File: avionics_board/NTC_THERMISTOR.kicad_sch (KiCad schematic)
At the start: 2 parts

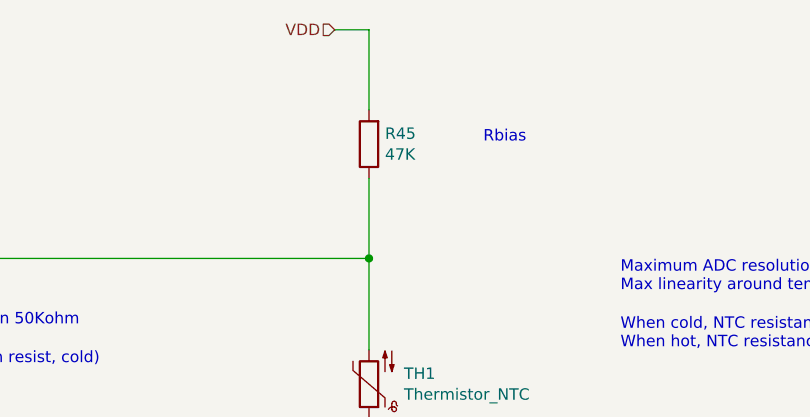
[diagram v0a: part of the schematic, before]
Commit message: change form factor to 80x80 and cleanup pcb
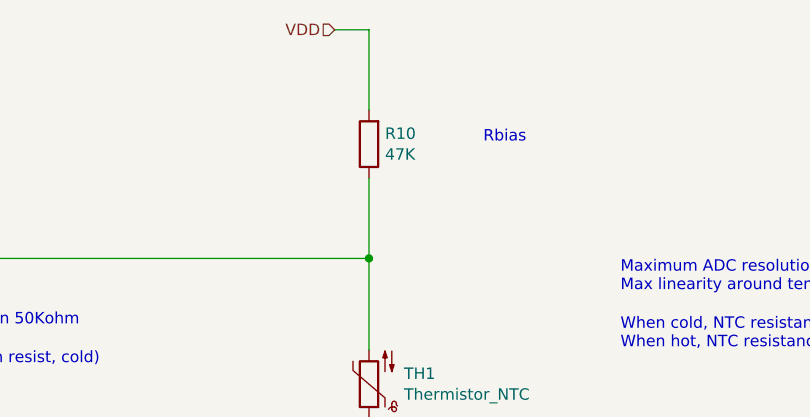
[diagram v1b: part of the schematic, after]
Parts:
- renumbered R45 to R10
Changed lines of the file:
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@@
 		(on_board yes)
 		(dnp no)
-		(property "Reference" "R45"
+		(property "Reference" "R10"
 			(at 122.428 47.0916 0)
 			(effects
@@
 			(project ""
 				(path "/f6cc00ab-17f1-4973-862f-7ac95fe70668/00000000-0000-0000-0000-00005ea31c93/00000000-0000-0000-0000-00005eab0b79/00000000-0000-0000-0000-00005eb419ee"
-					(reference "R45")
+					(reference "R10")
 					(unit 1)
 				)
 				(path "/f6cc00ab-17f1-4973-862f-7ac95fe70668/00000000-0000-0000-0000-00005ea31c93/00000000-0000-0000-0000-00005eab0b79/00000000-0000-0000-0000-00005ec0237f"
-					(reference "R46")
+					(reference "R11")
 					(unit 1)
 				)
 				(path "/f6cc00ab-17f1-4973-862f-7ac95fe70668/00000000-0000-0000-0000-00005ea31c93/00000000-0000-0000-0000-00005eab0b79/00000000-0000-0000-0000-00005ec02646"
-					(reference "R47")
+					(reference "R12")
 					(unit 1)
 				)
 				(path "/f6cc00ab-17f1-4973-862f-7ac95fe70668/00000000-0000-0000-0000-00005ea31c93/00000000-0000-0000-0000-00005eab0b79/00000000-0000-0000-0000-00005ec0264b"
-					(reference "R48")
+					(reference "R13")
 					(unit 1)
 				)
 				(path "/f6cc00ab-17f1-4973-862f-7ac95fe70668/00000000-0000-0000-0000-00005ea31c93/00000000-0000-0000-0000-00005eab0b79/00000000-0000-0000-0000-00005ec02e34"
-					(reference "R49")
+					(reference "R14")
 					(unit 1)
 				)
 				(path "/f6cc00ab-17f1-4973-862f-7ac95fe70668/00000000-0000-0000-0000-00005ea31c93/00000000-0000-0000-0000-00005eab0b79/00000000-0000-0000-0000-00005ec02e39"
-					(reference "R50")
+					(reference "R15")
 					(unit 1)
 				)
 				(path "/f6cc00ab-17f1-4973-862f-7ac95fe70668/00000000-0000-0000-0000-00005ea31c93/00000000-0000-0000-0000-00005eab0b79/00000000-0000-0000-0000-00005ec02e3e"
-					(reference "R51")
+					(reference "R16")
 					(unit 1)
 				)
 				(path "/f6cc00ab-17f1-4973-862f-7ac95fe70668/00000000-0000-0000-0000-00005ea31c93/00000000-0000-0000-0000-00005eab0b79/00000000-0000-0000-0000-00005ec02e43"
-					(reference "R52")
+					(reference "R17")
 					(unit 1)
 				)

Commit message: AV: small cleanup, USB, and CAN power
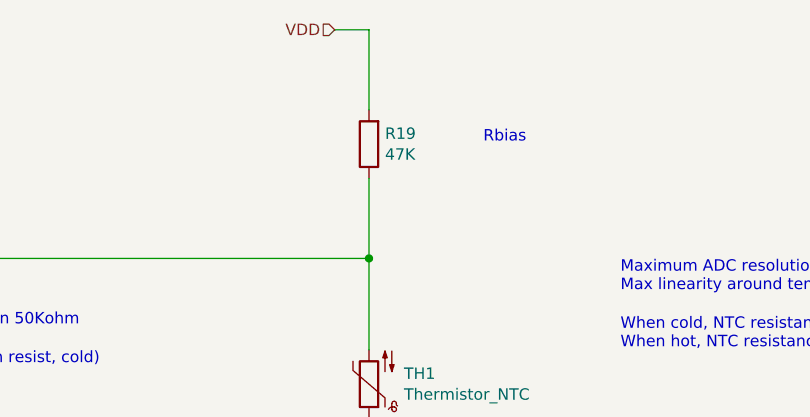
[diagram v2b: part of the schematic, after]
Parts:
- renumbered R10 to R19
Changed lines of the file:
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@@
 		(on_board yes)
 		(dnp no)
-		(property "Reference" "R10"
+		(property "Reference" "R19"
 			(at 122.428 47.0916 0)
 			(effects
@@
 			(project ""
 				(path "/f6cc00ab-17f1-4973-862f-7ac95fe70668/00000000-0000-0000-0000-00005ea31c93/00000000-0000-0000-0000-00005eab0b79/00000000-0000-0000-0000-00005eb419ee"
-					(reference "R10")
+					(reference "R19")
 					(unit 1)
 				)
 				(path "/f6cc00ab-17f1-4973-862f-7ac95fe70668/00000000-0000-0000-0000-00005ea31c93/00000000-0000-0000-0000-00005eab0b79/00000000-0000-0000-0000-00005ec0237f"
-					(reference "R11")
+					(reference "R20")
 					(unit 1)
 				)
 				(path "/f6cc00ab-17f1-4973-862f-7ac95fe70668/00000000-0000-0000-0000-00005ea31c93/00000000-0000-0000-0000-00005eab0b79/00000000-0000-0000-0000-00005ec02646"
-					(reference "R12")
+					(reference "R21")
 					(unit 1)
 				)
 				(path "/f6cc00ab-17f1-4973-862f-7ac95fe70668/00000000-0000-0000-0000-00005ea31c93/00000000-0000-0000-0000-00005eab0b79/00000000-0000-0000-0000-00005ec0264b"
-					(reference "R13")
+					(reference "R22")
 					(unit 1)
 				)
 				(path "/f6cc00ab-17f1-4973-862f-7ac95fe70668/00000000-0000-0000-0000-00005ea31c93/00000000-0000-0000-0000-00005eab0b79/00000000-0000-0000-0000-00005ec02e34"
-					(reference "R14")
+					(reference "R23")
 					(unit 1)
 				)
 				(path "/f6cc00ab-17f1-4973-862f-7ac95fe70668/00000000-0000-0000-0000-00005ea31c93/00000000-0000-0000-0000-00005eab0b79/00000000-0000-0000-0000-00005ec02e39"
-					(reference "R15")
+					(reference "R24")
 					(unit 1)
 				)
 				(path "/f6cc00ab-17f1-4973-862f-7ac95fe70668/00000000-0000-0000-0000-00005ea31c93/00000000-0000-0000-0000-00005eab0b79/00000000-0000-0000-0000-00005ec02e3e"
-					(reference "R16")
+					(reference "R25")
 					(unit 1)
 				)
 				(path "/f6cc00ab-17f1-4973-862f-7ac95fe70668/00000000-0000-0000-0000-00005ea31c93/00000000-0000-0000-0000-00005eab0b79/00000000-0000-0000-0000-00005ec02e43"
-					(reference "R17")
+					(reference "R26")
 					(unit 1)
 				)

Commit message: replace nearly all buck converters with boost buck (missing is 5raw
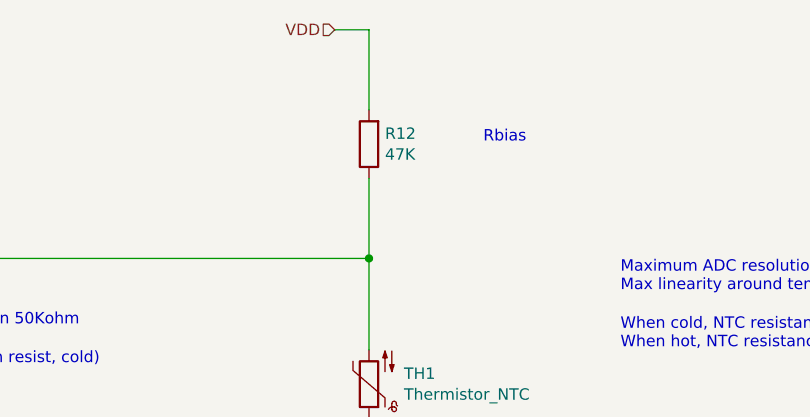
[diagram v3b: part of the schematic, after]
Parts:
- renumbered R19 to R12
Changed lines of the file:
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@@
 		(on_board yes)
 		(dnp no)
-		(property "Reference" "R19"
+		(property "Reference" "R12"
 			(at 122.428 47.0916 0)
 			(effects
@@
 			(project ""
 				(path "/f6cc00ab-17f1-4973-862f-7ac95fe70668/00000000-0000-0000-0000-00005ea31c93/00000000-0000-0000-0000-00005eab0b79/00000000-0000-0000-0000-00005eb419ee"
+					(reference "R12")
+					(unit 1)
+				)
+				(path "/f6cc00ab-17f1-4973-862f-7ac95fe70668/00000000-0000-0000-0000-00005ea31c93/00000000-0000-0000-0000-00005eab0b79/00000000-0000-0000-0000-00005ec0237f"
+					(reference "R13")
+					(unit 1)
+				)
+				(path "/f6cc00ab-17f1-4973-862f-7ac95fe70668/00000000-0000-0000-0000-00005ea31c93/00000000-0000-0000-0000-00005eab0b79/00000000-0000-0000-0000-00005ec02646"
+					(reference "R14")
+					(unit 1)
+				)
+				(path "/f6cc00ab-17f1-4973-862f-7ac95fe70668/00000000-0000-0000-0000-00005ea31c93/00000000-0000-0000-0000-00005eab0b79/00000000-0000-0000-0000-00005ec0264b"
+					(reference "R15")
+					(unit 1)
+				)
+				(path "/f6cc00ab-17f1-4973-862f-7ac95fe70668/00000000-0000-0000-0000-00005ea31c93/00000000-0000-0000-0000-00005eab0b79/00000000-0000-0000-0000-00005ec02e34"
+					(reference "R16")
+					(unit 1)
+				)
+				(path "/f6cc00ab-17f1-4973-862f-7ac95fe70668/00000000-0000-0000-0000-00005ea31c93/00000000-0000-0000-0000-00005eab0b79/00000000-0000-0000-0000-00005ec02e39"
+					(reference "R17")
+					(unit 1)
+				)
+				(path "/f6cc00ab-17f1-4973-862f-7ac95fe70668/00000000-0000-0000-0000-00005ea31c93/00000000-0000-0000-0000-00005eab0b79/00000000-0000-0000-0000-00005ec02e3e"
+					(reference "R18")
+					(unit 1)
+				)
+				(path "/f6cc00ab-17f1-4973-862f-7ac95fe70668/00000000-0000-0000-0000-00005ea31c93/00000000-0000-0000-0000-00005eab0b79/00000000-0000-0000-0000-00005ec02e43"
 					(reference "R19")
 					(unit 1)
 				)
-				(path "/f6cc00ab-17f1-4973-862f-7ac95fe70668/00000000-0000-0000-0000-00005ea31c93/00000000-0000-0000-0000-00005eab0b79/00000000-0000-0000-0000-00005ec0237f"
-					(reference "R20")
-					(unit 1)
-				)
-				(path "/f6cc00ab-17f1-4973-862f-7ac95fe70668/00000000-0000-0000-0000-00005ea31c93/00000000-0000-0000-0000-00005eab0b79/00000000-0000-0000-0000-00005ec02646"
-					(reference "R21")
-					(unit 1)
-				)
-				(path "/f6cc00ab-17f1-4973-862f-7ac95fe70668/00000000-0000-0000-0000-00005ea31c93/00000000-0000-0000-0000-00005eab0b79/00000000-0000-0000-0000-00005ec0264b"
-					(reference "R22")
-					(unit 1)
-				)
-				(path "/f6cc00ab-17f1-4973-862f-7ac95fe70668/00000000-0000-0000-0000-00005ea31c93/00000000-0000-0000-0000-00005eab0b79/00000000-0000-0000-0000-00005ec02e34"
-					(reference "R23")
-					(unit 1)
-				)
-				(path "/f6cc00ab-17f1-4973-862f-7ac95fe70668/00000000-0000-0000-0000-00005ea31c93/00000000-0000-0000-0000-00005eab0b79/00000000-0000-0000-0000-00005ec02e39"
-					(reference "R24")
-					(unit 1)
-				)
-				(path "/f6cc00ab-17f1-4973-862f-7ac95fe70668/00000000-0000-0000-0000-00005ea31c93/00000000-0000-0000-0000-00005eab0b79/00000000-0000-0000-0000-00005ec02e3e"
-					(reference "R25")
-					(unit 1)
-				)
-				(path "/f6cc00ab-17f1-4973-862f-7ac95fe70668/00000000-0000-0000-0000-00005ea31c93/00000000-0000-0000-0000-00005eab0b79/00000000-0000-0000-0000-00005ec02e43"
-					(reference "R26")
-					(unit 1)
-				)

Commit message: interim checkin before streamlining AVI
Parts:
- R12: Mfr. # CR0603-FX-4702ELF -> (none)
- TH1: Mfr. # NXFT15WB473FA2B150 -> (none); Part Number (none) -> NXFT15WB473FA2B150
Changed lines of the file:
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@@
-			)
-		)
-		(property "Mfr. #" "NXFT15WB473FA2B150"
-			(at 120.65 74.93 90)
-			(effects
-				(font
-					(size 1.27 1.27)
-				)
-				(hide yes)
 			)
 		)
@@
 		)
 		(property "Alt" ""
+			(at 120.65 74.93 0)
+			(effects
+				(font
+					(size 1.27 1.27)
+				)
+				(hide yes)
+			)
+		)
+		(property "Part Number" "NXFT15WB473FA2B150"
 			(at 120.65 74.93 0)
 			(effects
@@
 			(at 120.65 48.26 0)
 			(effects
-				(font
-					(size 1.27 1.27)
-				)
-				(hide yes)
-			)
-		)
-		(property "Mfr. #" "CR0603-FX-4702ELF"
-			(at 120.65 48.26 0)
-			(effects

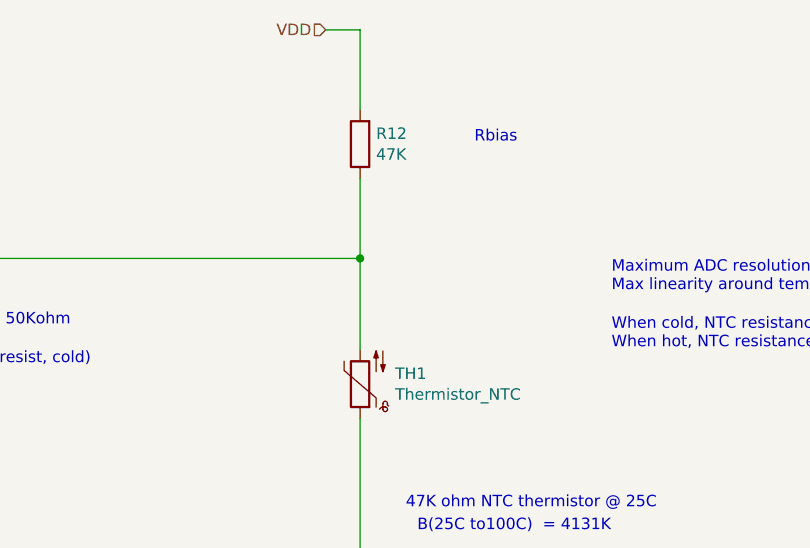
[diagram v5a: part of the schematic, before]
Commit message: refactor AVI into nicer hierarchical components
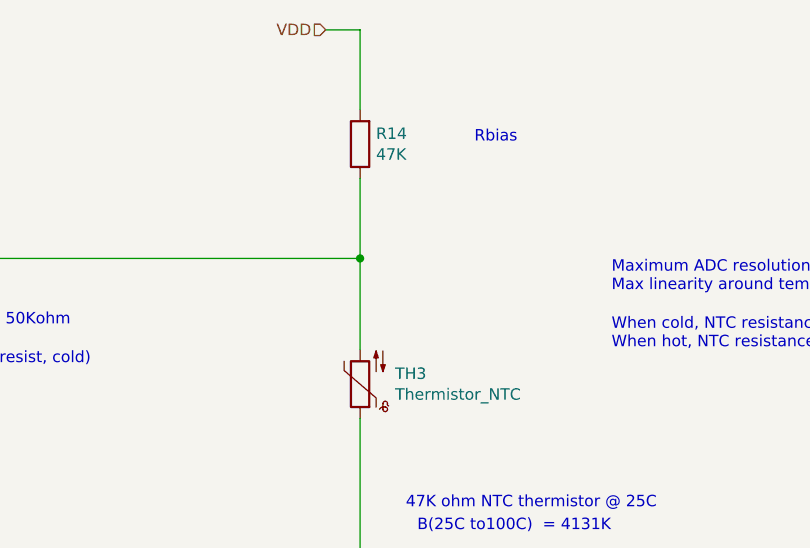
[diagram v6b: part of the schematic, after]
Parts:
- renumbered R12 to R14, TH1 to TH3
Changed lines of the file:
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@@
 		(on_board yes)
 		(dnp no)
-		(property "Reference" "TH1"
+		(property "Reference" "TH3"
 			(at 124.5362 73.7616 0)
 			(effects
@@
 		)
 		(instances
-			(project ""
-				(path "/f6cc00ab-17f1-4973-862f-7ac95fe70668/00000000-0000-0000-0000-00005ea31c93/00000000-0000-0000-0000-00005eab0b79/00000000-0000-0000-0000-00005eb419ee"
+			(project "AVIONICS_BOARD"
+				(path "/f6cc00ab-17f1-4973-862f-7ac95fe70668/4b32b6cb-e4ab-41a8-b61c-93e0ce1b94ae/00000000-0000-0000-0000-00005eb419ee"
 					(reference "TH1")
 					(unit 1)
 				)
-				(path "/f6cc00ab-17f1-4973-862f-7ac95fe70668/00000000-0000-0000-0000-00005ea31c93/00000000-0000-0000-0000-00005eab0b79/00000000-0000-0000-0000-00005ec0237f"
+				(path "/f6cc00ab-17f1-4973-862f-7ac95fe70668/4b32b6cb-e4ab-41a8-b61c-93e0ce1b94ae/00000000-0000-0000-0000-00005ec0237f"
 					(reference "TH2")
 					(unit 1)
 				)
-				(path "/f6cc00ab-17f1-4973-862f-7ac95fe70668/00000000-0000-0000-0000-00005ea31c93/00000000-0000-0000-0000-00005eab0b79/00000000-0000-0000-0000-00005ec02646"
+				(path "/f6cc00ab-17f1-4973-862f-7ac95fe70668/4b32b6cb-e4ab-41a8-b61c-93e0ce1b94ae/00000000-0000-0000-0000-00005ec02646"
 					(reference "TH3")
 					(unit 1)
 				)
-				(path "/f6cc00ab-17f1-4973-862f-7ac95fe70668/00000000-0000-0000-0000-00005ea31c93/00000000-0000-0000-0000-00005eab0b79/00000000-0000-0000-0000-00005ec0264b"
+				(path "/f6cc00ab-17f1-4973-862f-7ac95fe70668/4b32b6cb-e4ab-41a8-b61c-93e0ce1b94ae/00000000-0000-0000-0000-00005ec0264b"
 					(reference "TH4")
 					(unit 1)
 				)
-				(path "/f6cc00ab-17f1-4973-862f-7ac95fe70668/00000000-0000-0000-0000-00005ea31c93/00000000-0000-0000-0000-00005eab0b79/00000000-0000-0000-0000-00005ec02e34"
+				(path "/f6cc00ab-17f1-4973-862f-7ac95fe70668/4b32b6cb-e4ab-41a8-b61c-93e0ce1b94ae/00000000-0000-0000-0000-00005ec02e34"
 					(reference "TH5")
 					(unit 1)
 				)
-				(path "/f6cc00ab-17f1-4973-862f-7ac95fe70668/00000000-0000-0000-0000-00005ea31c93/00000000-0000-0000-0000-00005eab0b79/00000000-0000-0000-0000-00005ec02e39"
+				(path "/f6cc00ab-17f1-4973-862f-7ac95fe70668/4b32b6cb-e4ab-41a8-b61c-93e0ce1b94ae/00000000-0000-0000-0000-00005ec02e39"
 					(reference "TH6")
 					(unit 1)
 				)
-				(path "/f6cc00ab-17f1-4973-862f-7ac95fe70668/00000000-0000-0000-0000-00005ea31c93/00000000-0000-0000-0000-00005eab0b79/00000000-0000-0000-0000-00005ec02e3e"
+				(path "/f6cc00ab-17f1-4973-862f-7ac95fe70668/4b32b6cb-e4ab-41a8-b61c-93e0ce1b94ae/00000000-0000-0000-0000-00005ec02e3e"
 					(reference "TH7")
 					(unit 1)
 				)
-				(path "/f6cc00ab-17f1-4973-862f-7ac95fe70668/00000000-0000-0000-0000-00005ea31c93/00000000-0000-0000-0000-00005eab0b79/00000000-0000-0000-0000-00005ec02e43"
+				(path "/f6cc00ab-17f1-4973-862f-7ac95fe70668/4b32b6cb-e4ab-41a8-b61c-93e0ce1b94ae/00000000-0000-0000-0000-00005ec02e43"
 					(reference "TH8")
 					(unit 1)
@@
 		(on_board yes)
 		(dnp no)
-		(property "Reference" "R12"
+		(property "Reference" "R14"
 			(at 122.428 47.0916 0)
 			(effects
@@
 		)
 		(instances
-			(project ""
-				(path "/f6cc00ab-17f1-4973-862f-7ac95fe70668/00000000-0000-0000-0000-00005ea31c93/00000000-0000-0000-0000-00005eab0b79/00000000-0000-0000-0000-00005eb419ee"
+			(project "AVIONICS_BOARD"
+				(path "/f6cc00ab-17f1-4973-862f-7ac95fe70668/4b32b6cb-e4ab-41a8-b61c-93e0ce1b94ae/00000000-0000-0000-0000-00005eb419ee"
 					(reference "R12")
 					(unit 1)
 				)
-				(path "/f6cc00ab-17f1-4973-862f-7ac95fe70668/00000000-0000-0000-0000-00005ea31c93/00000000-0000-0000-0000-00005eab0b79/00000000-0000-0000-0000-00005ec0237f"
+				(path "/f6cc00ab-17f1-4973-862f-7ac95fe70668/4b32b6cb-e4ab-41a8-b61c-93e0ce1b94ae/00000000-0000-0000-0000-00005ec0237f"
 					(reference "R13")
 					(unit 1)
 				)
-				(path "/f6cc00ab-17f1-4973-862f-7ac95fe70668/00000000-0000-0000-0000-00005ea31c93/00000000-0000-0000-0000-00005eab0b79/00000000-0000-0000-0000-00005ec02646"
+				(path "/f6cc00ab-17f1-4973-862f-7ac95fe70668/4b32b6cb-e4ab-41a8-b61c-93e0ce1b94ae/00000000-0000-0000-0000-00005ec02646"
 					(reference "R14")
 					(unit 1)
 				)
-				(path "/f6cc00ab-17f1-4973-862f-7ac95fe70668/00000000-0000-0000-0000-00005ea31c93/00000000-0000-0000-0000-00005eab0b79/00000000-0000-0000-0000-00005ec0264b"
+				(path "/f6cc00ab-17f1-4973-862f-7ac95fe70668/4b32b6cb-e4ab-41a8-b61c-93e0ce1b94ae/00000000-0000-0000-0000-00005ec0264b"
 					(reference "R15")
 					(unit 1)
 				)
-				(path "/f6cc00ab-17f1-4973-862f-7ac95fe70668/00000000-0000-0000-0000-00005ea31c93/00000000-0000-0000-0000-00005eab0b79/00000000-0000-0000-0000-00005ec02e34"
+				(path "/f6cc00ab-17f1-4973-862f-7ac95fe70668/4b32b6cb-e4ab-41a8-b61c-93e0ce1b94ae/00000000-0000-0000-0000-00005ec02e34"
 					(reference "R16")
 					(unit 1)
 				)
-				(path "/f6cc00ab-17f1-4973-862f-7ac95fe70668/00000000-0000-0000-0000-00005ea31c93/00000000-0000-0000-0000-00005eab0b79/00000000-0000-0000-0000-00005ec02e39"
+				(path "/f6cc00ab-17f1-4973-862f-7ac95fe70668/4b32b6cb-e4ab-41a8-b61c-93e0ce1b94ae/00000000-0000-0000-0000-00005ec02e39"
 					(reference "R17")
 					(unit 1)
 				)
-				(path "/f6cc00ab-17f1-4973-862f-7ac95fe70668/00000000-0000-0000-0000-00005ea31c93/00000000-0000-0000-0000-00005eab0b79/00000000-0000-0000-0000-00005ec02e3e"
+				(path "/f6cc00ab-17f1-4973-862f-7ac95fe70668/4b32b6cb-e4ab-41a8-b61c-93e0ce1b94ae/00000000-0000-0000-0000-00005ec02e3e"
 					(reference "R18")
 					(unit 1)
 				)
-				(path "/f6cc00ab-17f1-4973-862f-7ac95fe70668/00000000-0000-0000-0000-00005ea31c93/00000000-0000-0000-0000-00005eab0b79/00000000-0000-0000-0000-00005ec02e43"
+				(path "/f6cc00ab-17f1-4973-862f-7ac95fe70668/4b32b6cb-e4ab-41a8-b61c-93e0ce1b94ae/00000000-0000-0000-0000-00005ec02e43"
 					(reference "R19")
 					(unit 1)

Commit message: AVI assigning interrupts
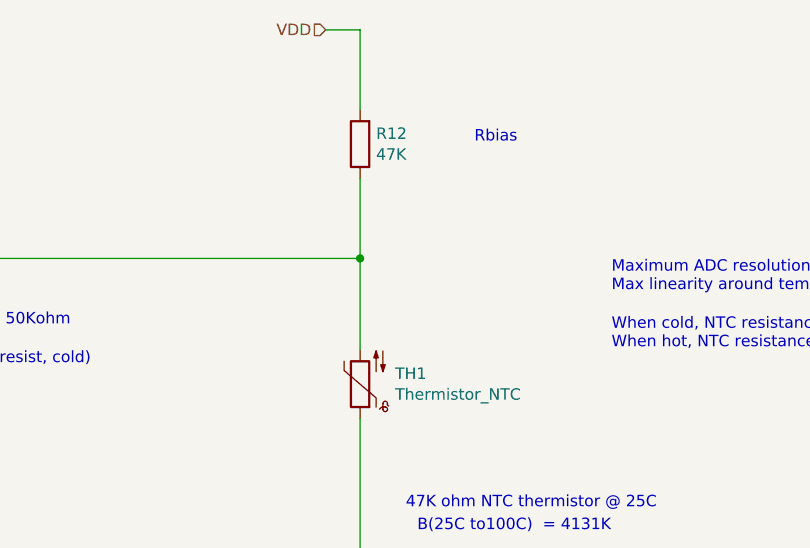
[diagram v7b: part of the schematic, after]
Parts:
- renumbered R14 to R12, TH3 to TH1
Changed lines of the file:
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@@
 		(on_board yes)
 		(dnp no)
-		(property "Reference" "TH3"
+		(property "Reference" "TH1"
 			(at 124.5362 73.7616 0)
 			(effects
@@
 		(on_board yes)
 		(dnp no)
-		(property "Reference" "R14"
+		(property "Reference" "R12"
 			(at 122.428 47.0916 0)
 			(effects

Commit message: reconcile BOMS for AVI. SCI and AUX
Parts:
- R12: footprint Resistor_SMD:R_0603_1608Metric_Pad0.98x0.95mm_HandSolder -> Resistor_SMD:R_0402_1005Metric_Pad0.72x0.64mm_HandSolder; Manufacturer (none) -> YAGEO; Part Number (none) -> RC0402FR-0747KL; Tolerance (none) -> 1
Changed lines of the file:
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@@
 			)
 		)
-		(property "Footprint" "Resistor_SMD:R_0603_1608Metric_Pad0.98x0.95mm_HandSolder"
+		(property "Footprint" "Resistor_SMD:R_0402_1005Metric_Pad0.72x0.64mm_HandSolder"
 			(at 122.428 48.26 90)
 			(effects
@@
 			)
 		)
-		(property "Datasheet" "https://www.bourns.com/docs/Product-Datasheets/CHPREZTR.pdf"
+		(property "Datasheet" "https://www.yageo.com/upload/media/product/products/datasheet/rchip/PYu-RC_Group_51_RoHS_L_12.pdf"
 			(at 120.65 48.26 0)
 			(effects
@@
 			(at 120.65 48.26 0)
 			(effects
+				(font
+					(size 1.27 1.27)
+				)
+				(hide yes)
+			)
+		)
+		(property "Manufacturer" "YAGEO"
+			(at 120.65 48.26 0)
+			(effects
+				(font
+					(size 1.27 1.27)
+				)
+				(hide yes)
+			)
+		)
+		(property "Part Number" "RC0402FR-0747KL"
+			(at 120.65 48.26 0)
+			(effects
+				(font
+					(size 1.27 1.27)
+				)
+				(hide yes)
+			)
+		)
+		(property "Tolerance" "1"
+			(at 120.65 48.26 0)
+			(effects
